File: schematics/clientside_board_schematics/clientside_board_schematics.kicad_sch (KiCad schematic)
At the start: 23 parts, among them J1 12V Power Input, J10 Keylock Switch Connector, J2 UART Connector, J3 MV1 Connector, J4 Comm Status LED, J5 12V Output, J6 Fire Button Connector, J7 5V Output, J8 LCD Connector, J9 Potentiometer Connector, T1 VXO7805-1000

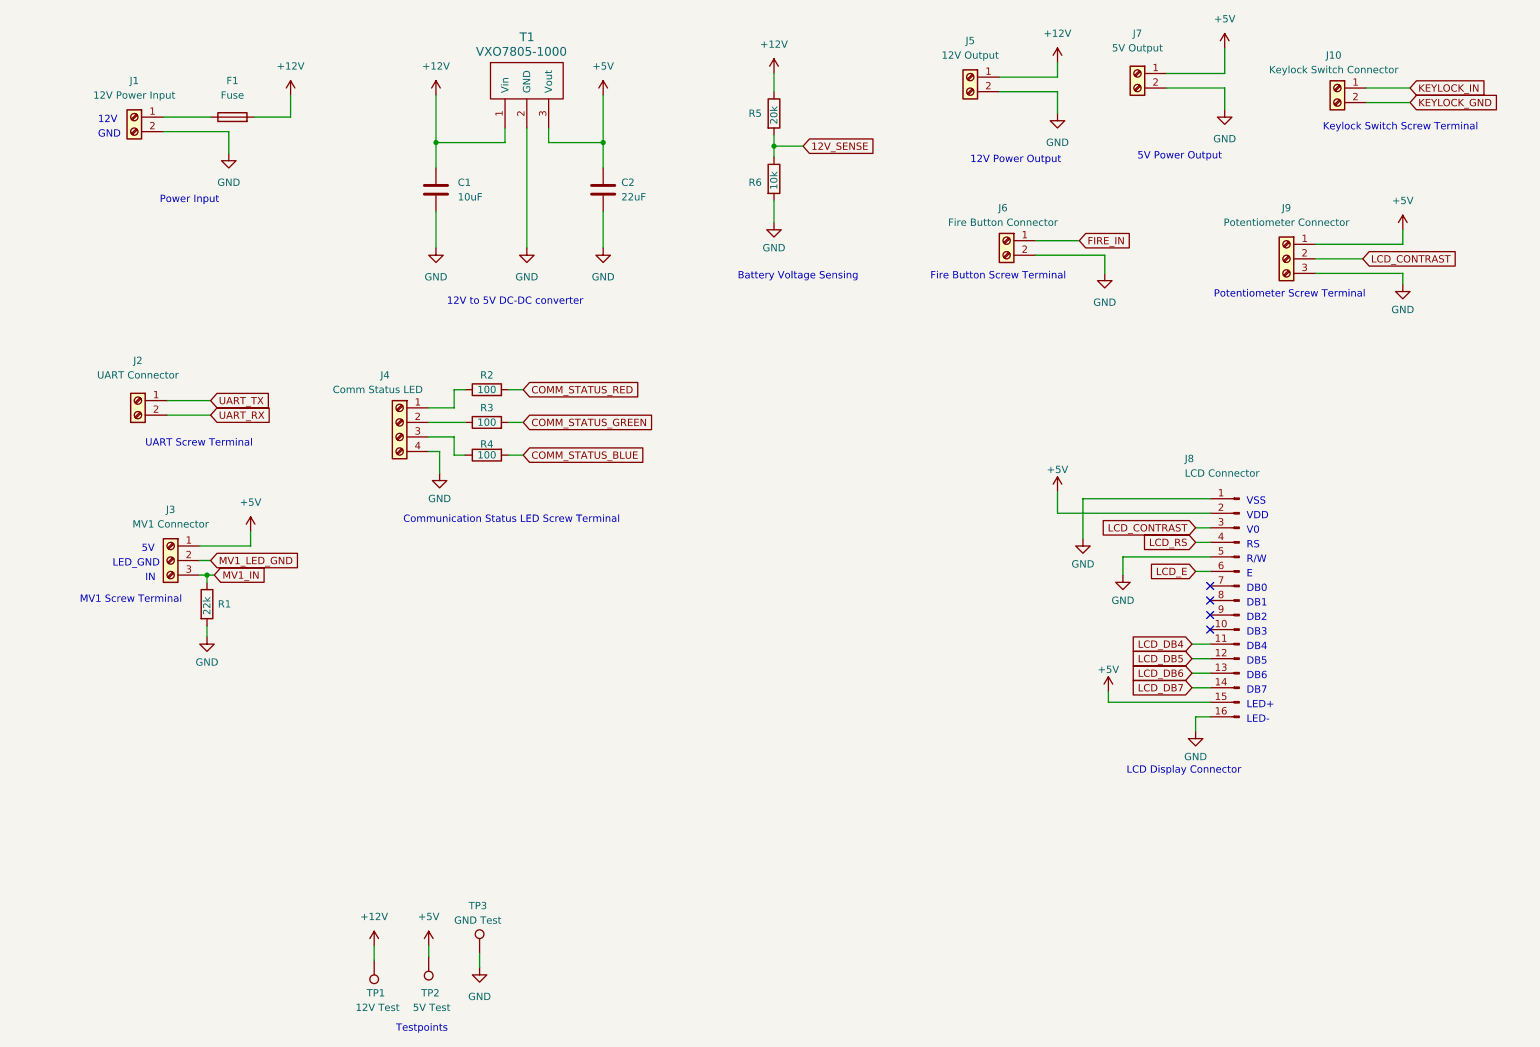
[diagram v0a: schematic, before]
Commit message: Complete client-side board schematic
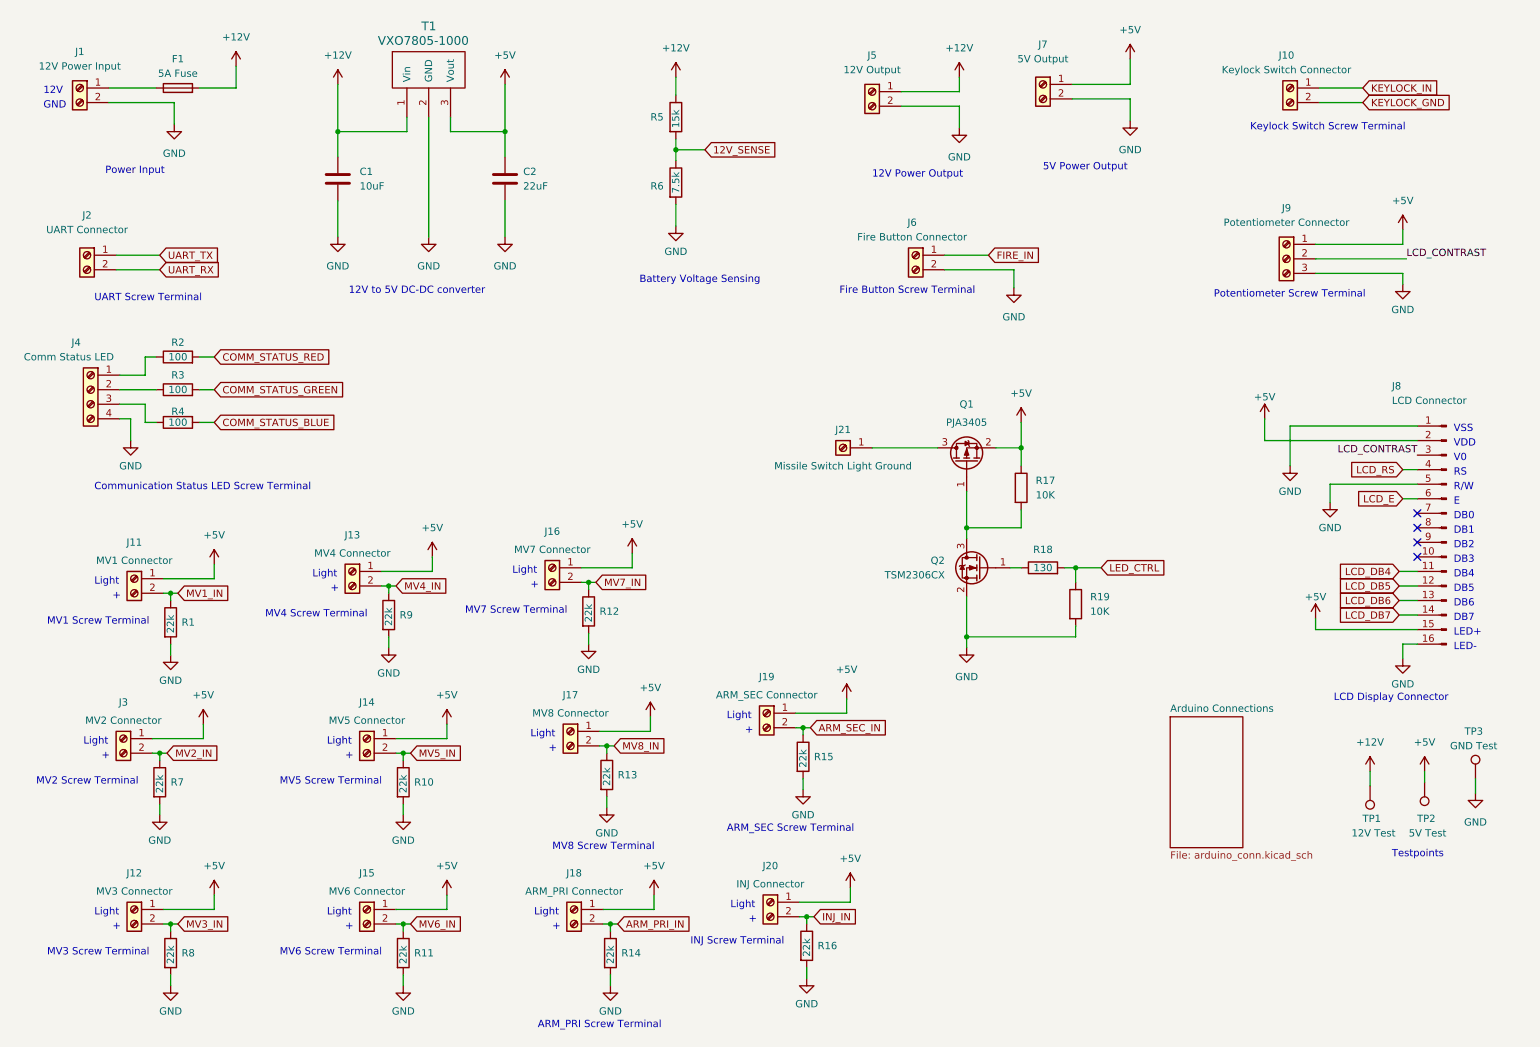
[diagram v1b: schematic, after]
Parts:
- removed J3: MV1 Connector, symbol Connector:Screw_Terminal_01x03
- added J11: MV1 Connector, symbol Connector:Screw_Terminal_01x02
- added J12: MV3 Connector, symbol Connector:Screw_Terminal_01x02
- added J13: MV4 Connector, symbol Connector:Screw_Terminal_01x02
- added J14: MV5 Connector, symbol Connector:Screw_Terminal_01x02
- added J15: MV6 Connector, symbol Connector:Screw_Terminal_01x02
- added J16: MV7 Connector, symbol Connector:Screw_Terminal_01x02
- added J17: MV8 Connector, symbol Connector:Screw_Terminal_01x02
- added J18: ARM_PRI Connector, symbol Connector:Screw_Terminal_01x02
- added J19: ARM_SEC Connector, symbol Connector:Screw_Terminal_01x02
- added J20: INJ Connector, symbol Connector:Screw_Terminal_01x02
- added J21: Missile Switch Light Ground, symbol Connector:Screw_Terminal_01x01
- added J3: MV2 Connector, symbol Connector:Screw_Terminal_01x02
- added Q1: PJA3405, symbol Device:Q_PMOS_GSD
- added Q2: TSM2306CX, symbol Device:Q_NMOS_GSD
- added R10, R11, R12, R13, R14, R15, R16, R7, R8, R9: 22k, symbol Device:R
- added R17, R19: 10K, symbol Device:R
- added R18: 130, symbol Device:R
- F1: value Fuse -> 5A Fuse
- R5: value 20k -> 15k
- R6: value 10k -> 7.5k
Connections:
- net +5V: now also J11.1 (Pin_1), J12.1 (Pin_1), J13.1 (Pin_1), J14.1 (Pin_1), J15.1 (Pin_1), J16.1 (Pin_1), J17.1 (Pin_1), J18.1 (Pin_1), J19.1 (Pin_1), J20.1 (Pin_1), J3.1 (Pin_1), Q1.2 (S), R17.1
- net GND: now also Q2.2 (S), R10.2, R11.2, R12.2, R13.2, R14.2, R15.2, R16.2, R19.2, R7.2, R8.2, R9.2
- net MV1_IN: now also J11.2 (Pin_2)
- new net: J21.1 (Pin_1), Q1.3 (D)
- new net: Q2.1 (G), R18.1
- new net: Q1.1 (G), Q2.3 (D), R17.2
- new net ARM_PRI_IN: J18.2 (Pin_2), R14.1
- new net ARM_SEC_IN: J19.2 (Pin_2), R15.1
- new net INJ_IN: J20.2 (Pin_2), R16.1
- new net LED_CTRL: R18.2, R19.1
- new net MV2_IN: J3.2 (Pin_2), R7.1
- new net MV3_IN: J12.2 (Pin_2), R8.1
- new net MV4_IN: J13.2 (Pin_2), R9.1
- new net MV5_IN: J14.2 (Pin_2), R10.1
- new net MV6_IN: J15.2 (Pin_2), R11.1
- new net MV7_IN: J16.2 (Pin_2), R12.1
- new net MV8_IN: J17.2 (Pin_2), R13.1
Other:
- added sheet Arduino Connections (arduino_conn.kicad_sch)
- note added: "+"
- note added: "ARM_PRI Screw Terminal"
- note added: "ARM_SEC Screw Terminal"
- note added: "INJ Screw Terminal"
- note added: "Light"
- note added: "MV2 Screw Terminal"
- note added: "MV3 Screw Terminal"
- note added: "MV4 Screw Terminal"
- note added: "MV5 Screw Terminal"
- note added: "MV6 Screw Terminal"
- note added: "MV7 Screw Terminal"
- note added: "MV8 Screw Terminal"
- note removed: "5V"
- note removed: "IN"
- note removed: "LED_GND"
- moved on the sheet: C1, C2, F1, J1, J10, J2, J4, J5, J6, J7, J8, R1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

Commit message: Assign footprints to RLCS Client-side board
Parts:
- C1, C2: footprint (none) -> Capacitor_SMD:C_0805_2012Metric_Pad1.15x1.40mm_HandSolder
- F1: footprint (none) -> Fuse:Fuseholder_Clip-5x20mm_Littelfuse_111_Inline_P20.00x5.00mm_D1.05mm_Horizontal
- J1, J5, J7: footprint (none) -> TerminalBlock_Phoenix:TerminalBlock_Phoenix_MKDS-1,5-2-5.08_1x02_P5.08mm_Horizontal
- J10, J11, J12, J13, J14, J15, J16, J17, J18, J19, J20, J21, J3, J6: footprint (none) -> TerminalBlock_Phoenix:TerminalBlock_Phoenix_PT-1,5-2-3.5-H_1x02_P3.50mm_Horizontal
- J2: footprint (none) -> TerminalBlock_TE-Connectivity:TerminalBlock_TE_282834-2_1x02_P2.54mm_Horizontal
- J4: footprint (none) -> TerminalBlock_Phoenix:TerminalBlock_Phoenix_PT-1,5-4-3.5-H_1x04_P3.50mm_Horizontal
- J8: footprint (none) -> Connector_PinSocket_2.54mm:PinSocket_1x16_P2.54mm_Vertical
- J9: footprint (none) -> TerminalBlock_Phoenix:TerminalBlock_Phoenix_PT-1,5-3-3.5-H_1x03_P3.50mm_Horizontal
- Q1, Q2: footprint (none) -> Package_TO_SOT_SMD:SOT-23_Handsoldering
- R1, R10, R11, R12, R13, R14, R15, R16, R17, R18, R19, R2, R3, R4, R5, R6, R7, R8, R9: footprint (none) -> Resistor_SMD:R_0805_2012Metric_Pad1.20x1.40mm_HandSolder
- T1: footprint (none) -> rlcs_power_footprints:VXO78XX-1000
- TP1, TP2, TP3: footprint (none) -> Connector_PinSocket_2.00mm:PinSocket_1x01_P2.00mm_Vertical

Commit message: Fix schematic issue on Client-side board
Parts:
- removed J2: UART Connector, TerminalBlock_TE-Connectivity:TerminalBlock_TE_282834-2_1x02_P2.54mm_Horizontal, symbol Connector:Screw_Terminal_01x02
- added J2: UART Connector, symbol Connector:Screw_Terminal_01x04
- R1, R10, R11, R12, R13, R14, R15, R16, R17, R19, R5, R6, R7, R8, R9: symbol Device:R -> Device:R_US
- R18: value 130 -> 130R; symbol Device:R -> Device:R_US
- R2, R3, R4: value 100 -> 100R; symbol Device:R -> Device:R_US
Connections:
- net KEYLOCK_GND is gone; now on net GND: J10.2 (Pin_2)
- net +5V: now also J2.3 (Pin_3)
- net GND: now also J2.4 (Pin_4)
- net UART_RX: now also J2.2 (Pin_2)
- net UART_TX: now also J2.1 (Pin_1)

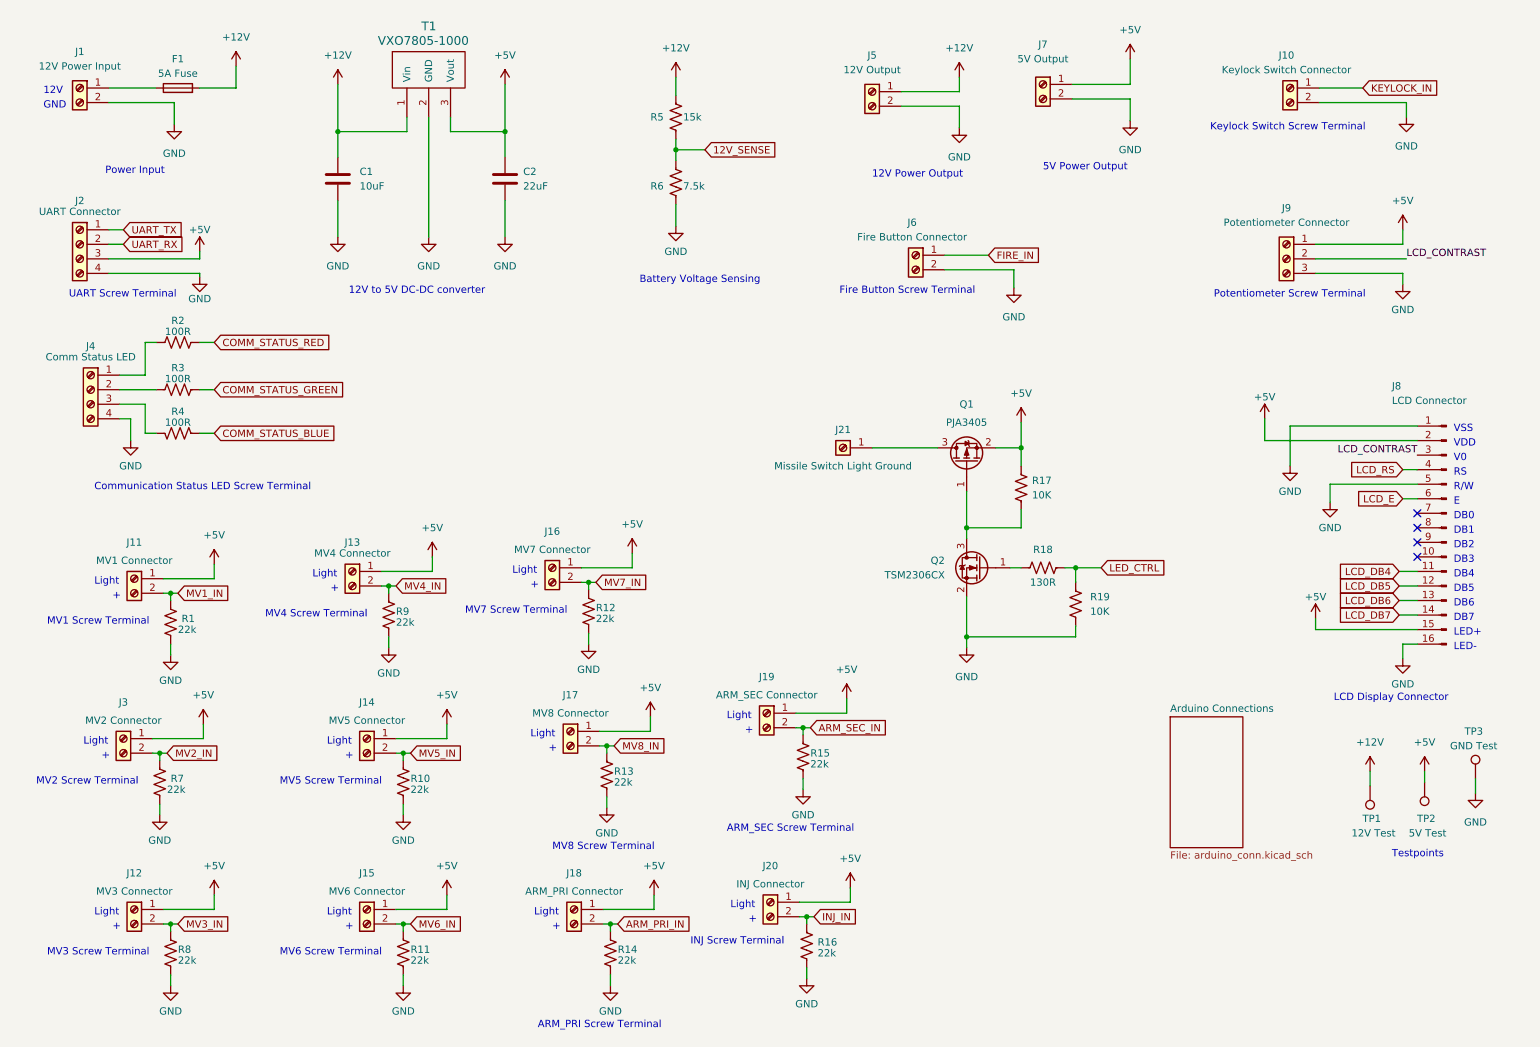
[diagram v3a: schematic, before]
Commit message: Split missile switch to a new sheet for Client-side board
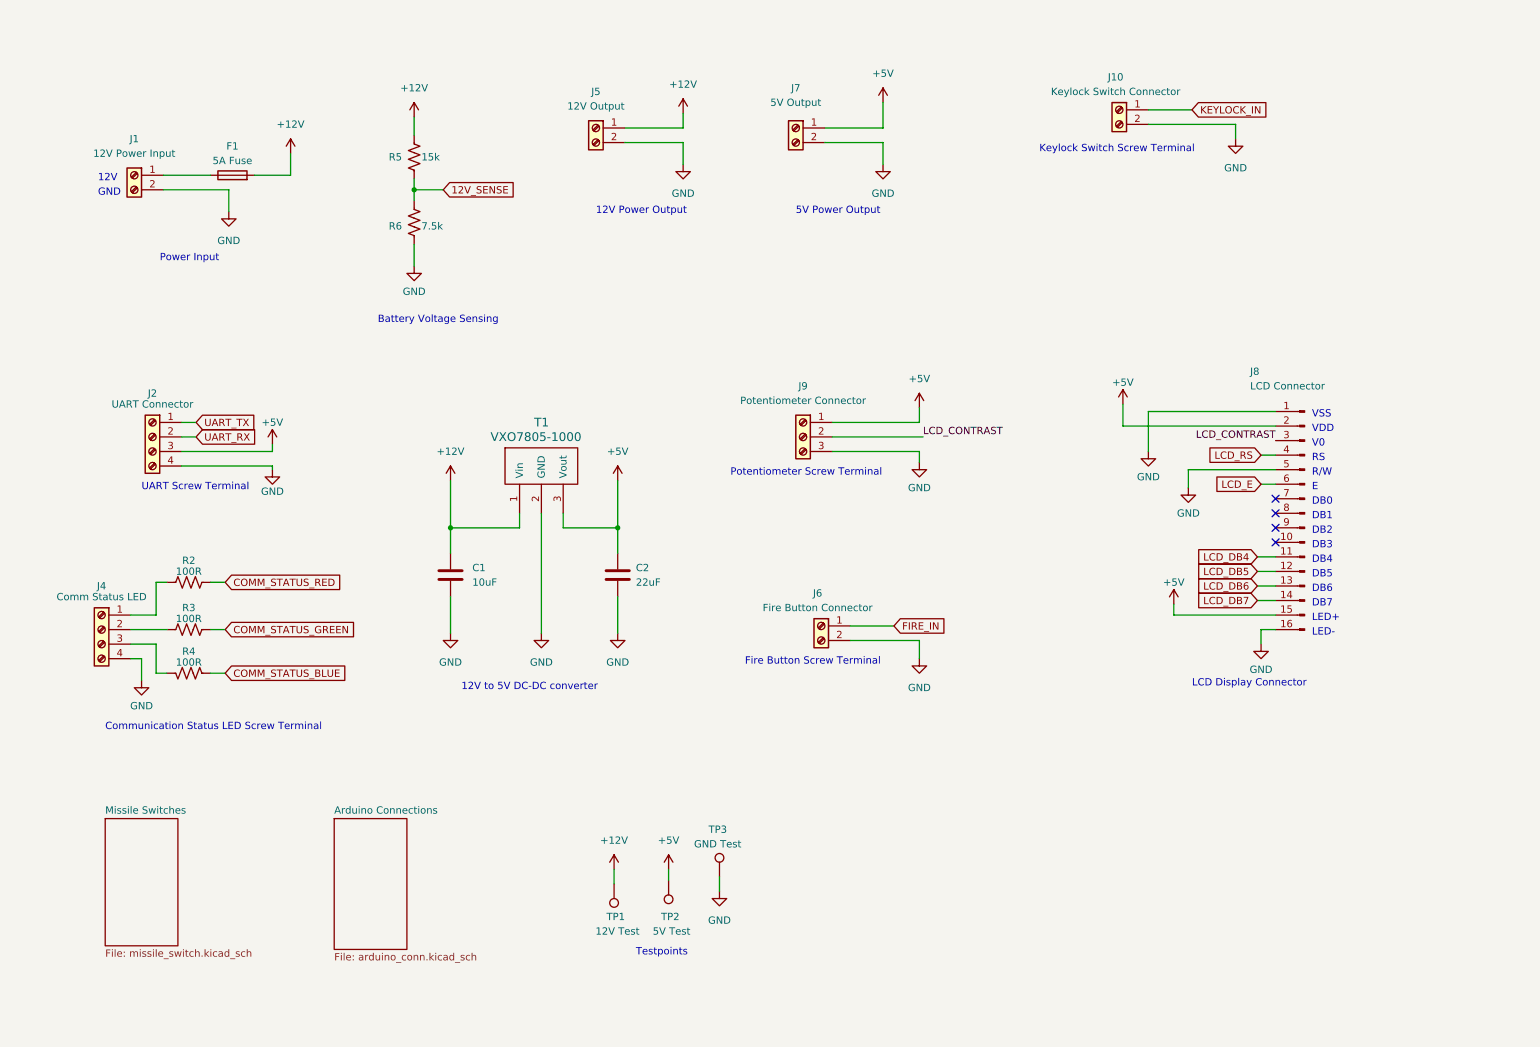
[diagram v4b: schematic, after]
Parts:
- removed J11: MV1 Connector, TerminalBlock_Phoenix:TerminalBlock_Phoenix_PT-1,5-2-3.5-H_1x02_P3.50mm_Horizontal, symbol Connector:Screw_Terminal_01x02
- removed J12: MV3 Connector, TerminalBlock_Phoenix:TerminalBlock_Phoenix_PT-1,5-2-3.5-H_1x02_P3.50mm_Horizontal, symbol Connector:Screw_Terminal_01x02
- removed J13: MV4 Connector, TerminalBlock_Phoenix:TerminalBlock_Phoenix_PT-1,5-2-3.5-H_1x02_P3.50mm_Horizontal, symbol Connector:Screw_Terminal_01x02
- removed J14: MV5 Connector, TerminalBlock_Phoenix:TerminalBlock_Phoenix_PT-1,5-2-3.5-H_1x02_P3.50mm_Horizontal, symbol Connector:Screw_Terminal_01x02
- removed J15: MV6 Connector, TerminalBlock_Phoenix:TerminalBlock_Phoenix_PT-1,5-2-3.5-H_1x02_P3.50mm_Horizontal, symbol Connector:Screw_Terminal_01x02
- removed J16: MV7 Connector, TerminalBlock_Phoenix:TerminalBlock_Phoenix_PT-1,5-2-3.5-H_1x02_P3.50mm_Horizontal, symbol Connector:Screw_Terminal_01x02
- removed J17: MV8 Connector, TerminalBlock_Phoenix:TerminalBlock_Phoenix_PT-1,5-2-3.5-H_1x02_P3.50mm_Horizontal, symbol Connector:Screw_Terminal_01x02
- removed J18: ARM_PRI Connector, TerminalBlock_Phoenix:TerminalBlock_Phoenix_PT-1,5-2-3.5-H_1x02_P3.50mm_Horizontal, symbol Connector:Screw_Terminal_01x02
- removed J19: ARM_SEC Connector, TerminalBlock_Phoenix:TerminalBlock_Phoenix_PT-1,5-2-3.5-H_1x02_P3.50mm_Horizontal, symbol Connector:Screw_Terminal_01x02
- removed J20: INJ Connector, TerminalBlock_Phoenix:TerminalBlock_Phoenix_PT-1,5-2-3.5-H_1x02_P3.50mm_Horizontal, symbol Connector:Screw_Terminal_01x02
- removed J21: Missile Switch Light Ground, TerminalBlock_Phoenix:TerminalBlock_Phoenix_PT-1,5-2-3.5-H_1x02_P3.50mm_Horizontal, symbol Connector:Screw_Terminal_01x01
- removed J3: MV2 Connector, TerminalBlock_Phoenix:TerminalBlock_Phoenix_PT-1,5-2-3.5-H_1x02_P3.50mm_Horizontal, symbol Connector:Screw_Terminal_01x02
- removed Q1: PJA3405, Package_TO_SOT_SMD:SOT-23_Handsoldering, symbol Device:Q_PMOS_GSD
- removed Q2: TSM2306CX, Package_TO_SOT_SMD:SOT-23_Handsoldering, symbol Device:Q_NMOS_GSD
- removed R1, R10, R11, R12, R13, R14, R15, R16, R7, R8, R9: 22k, Resistor_SMD:R_0805_2012Metric_Pad1.20x1.40mm_HandSolder, symbol Device:R_US
- removed R17, R19: 10K, Resistor_SMD:R_0805_2012Metric_Pad1.20x1.40mm_HandSolder, symbol Device:R_US
- removed R18: 130R, Resistor_SMD:R_0805_2012Metric_Pad1.20x1.40mm_HandSolder, symbol Device:R_US
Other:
- added sheet Missile Switches (missile_switch.kicad_sch)
- note removed: "+"
- note removed: "ARM_PRI Screw Terminal"
- note removed: "ARM_SEC Screw Terminal"
- note removed: "INJ Screw Terminal"
- note removed: "Light"
- note removed: "MV1 Screw Terminal"
- note removed: "MV2 Screw Terminal"
- note removed: "MV3 Screw Terminal"
- note removed: "MV4 Screw Terminal"
- note removed: "MV5 Screw Terminal"
- note removed: "MV6 Screw Terminal"
- note removed: "MV7 Screw Terminal"
- note removed: "MV8 Screw Terminal"
- moved on the sheet: C1, C2, F1, J1, J10, J2, J4, J5, J6, J7, J8, J9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
